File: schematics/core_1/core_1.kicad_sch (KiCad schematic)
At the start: 21 parts, among them U1 74LS00, U2 74LS04, U3 74LS109, U4 74LS02

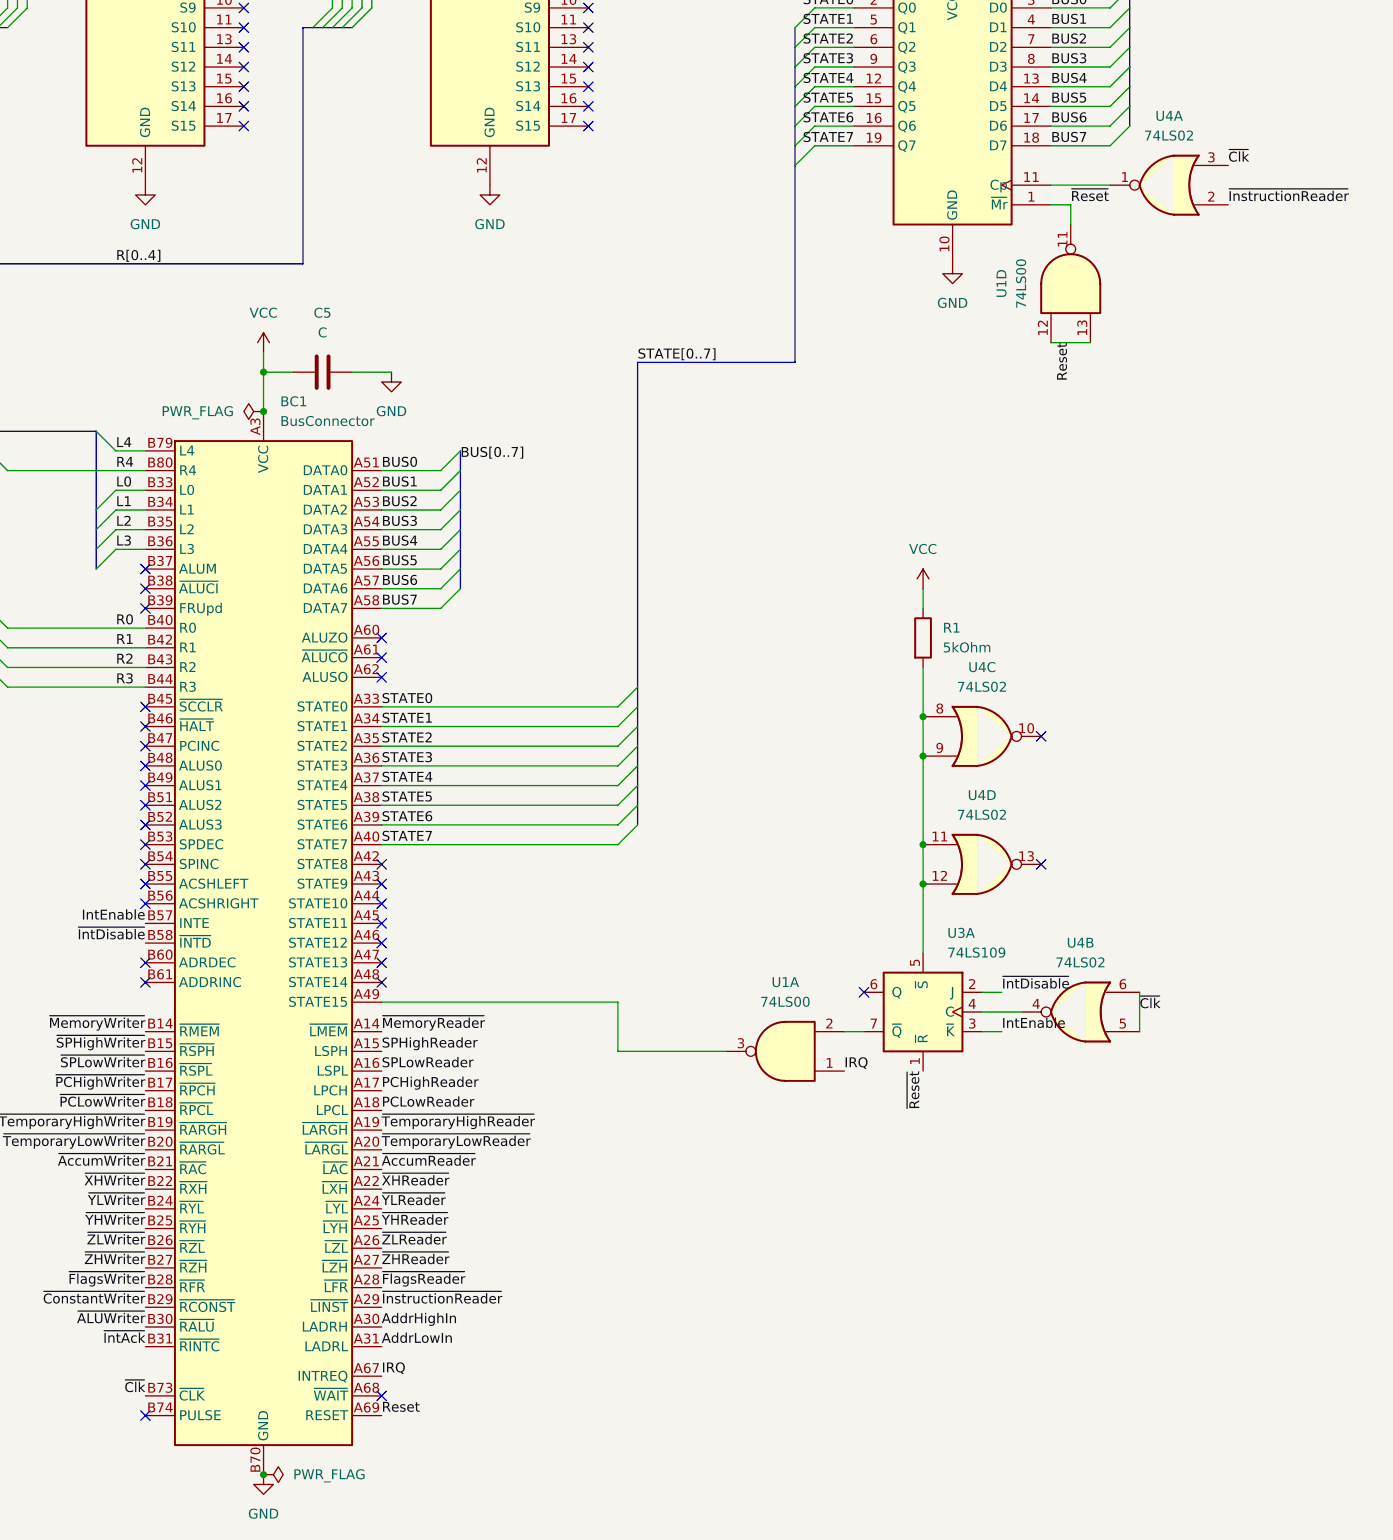
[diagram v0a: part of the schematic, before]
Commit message: Add test points in Core 1
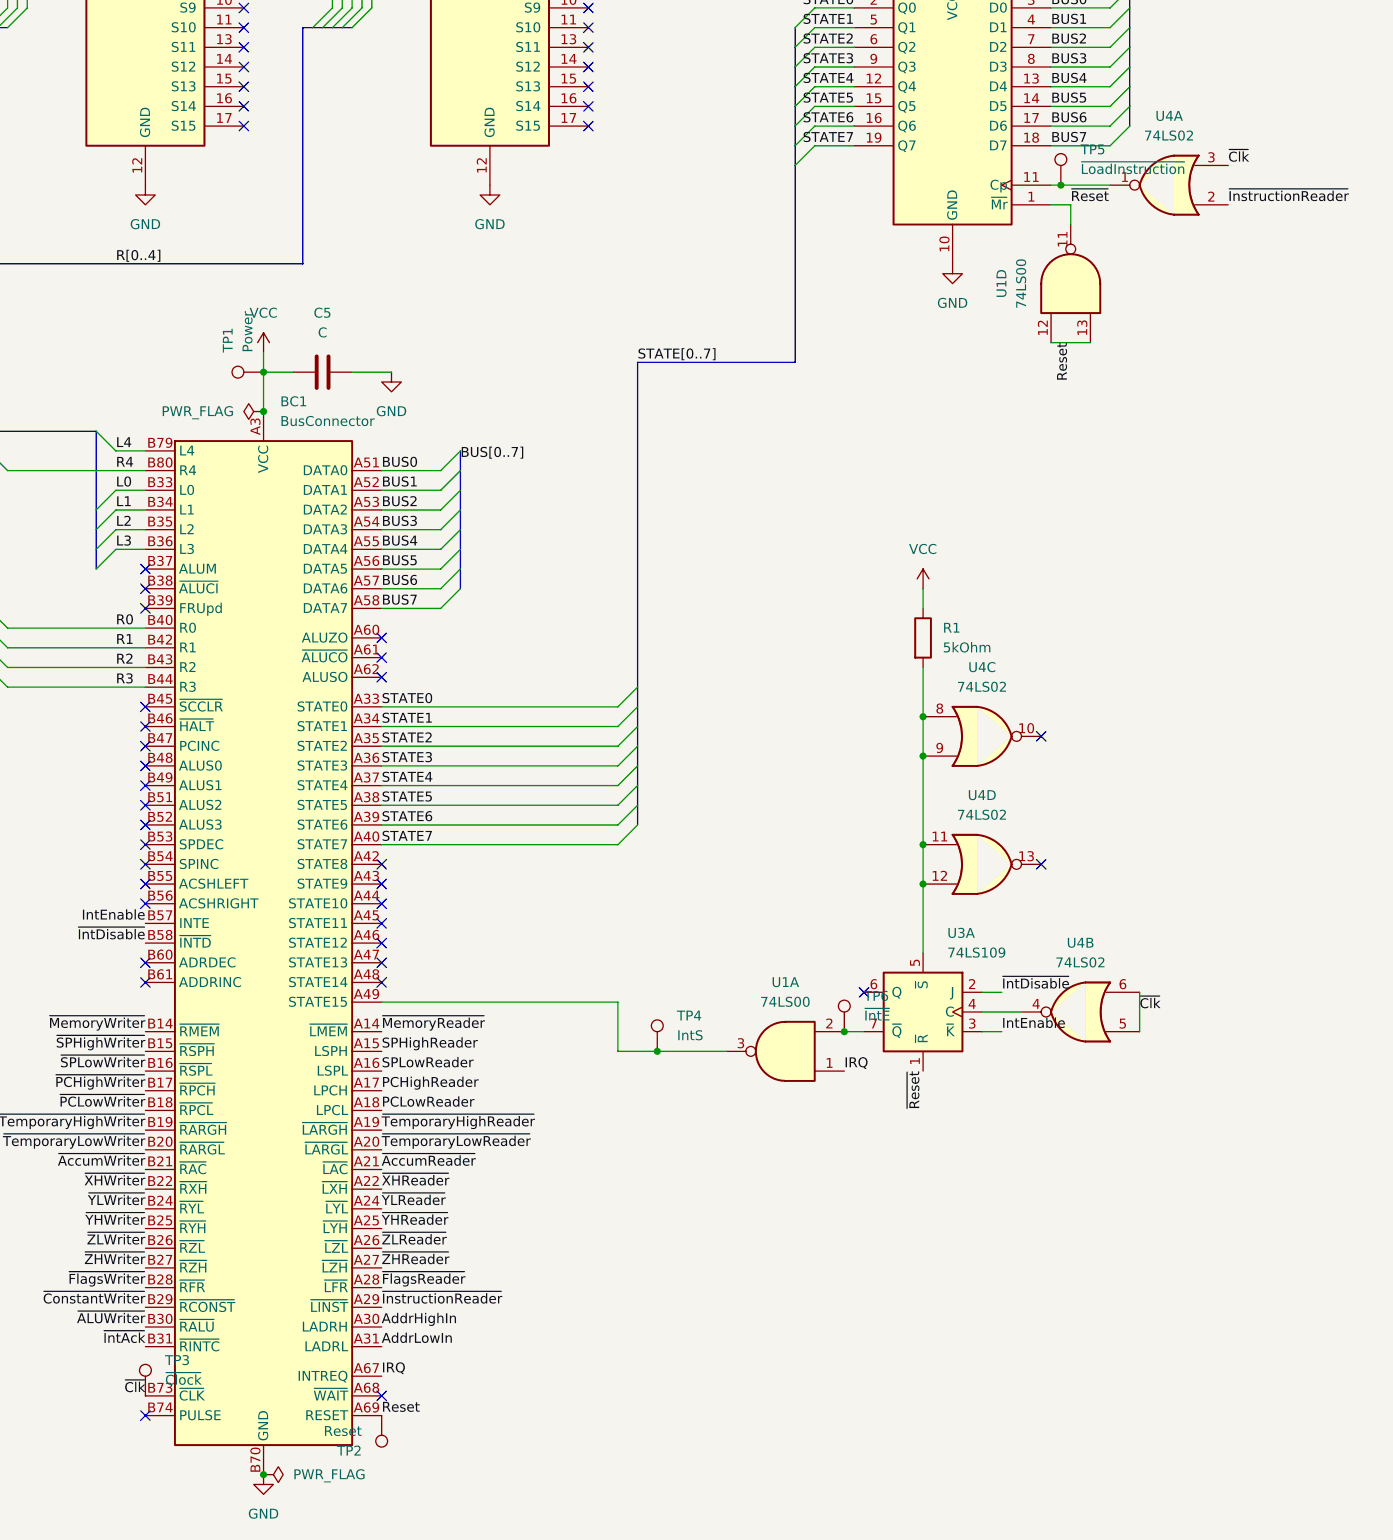
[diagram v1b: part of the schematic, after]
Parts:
- added TP1: Power, Connector_Pin:Pin_D1.0mm_L10.0mm, symbol Connector:TestPoint
- added TP2: Reset, Connector_Pin:Pin_D1.0mm_L10.0mm, symbol Connector:TestPoint
- added TP3: ~{Clock}, Connector_Pin:Pin_D1.0mm_L10.0mm, symbol Connector:TestPoint
- added TP4: IntS, Connector_Pin:Pin_D1.0mm_L10.0mm, symbol Connector:TestPoint
- added TP5: ~{LoadInstruction}, Connector_Pin:Pin_D1.0mm_L10.0mm, symbol Connector:TestPoint
- added TP6: ~{IntE}, Connector_Pin:Pin_D1.0mm_L10.0mm, symbol Connector:TestPoint
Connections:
- net Reset: now also TP2.1
- net VCC: now also TP1.1
- net ~{Clk}: now also TP3.1
- net at INSTRUCTION1.11 (Cp), U4.1: now also TP5.1
- net at BC1.A49 (STATE15), U1.3: now also TP4.1
- net at U1.2, U3.7 (~{Q}): now also TP6.1

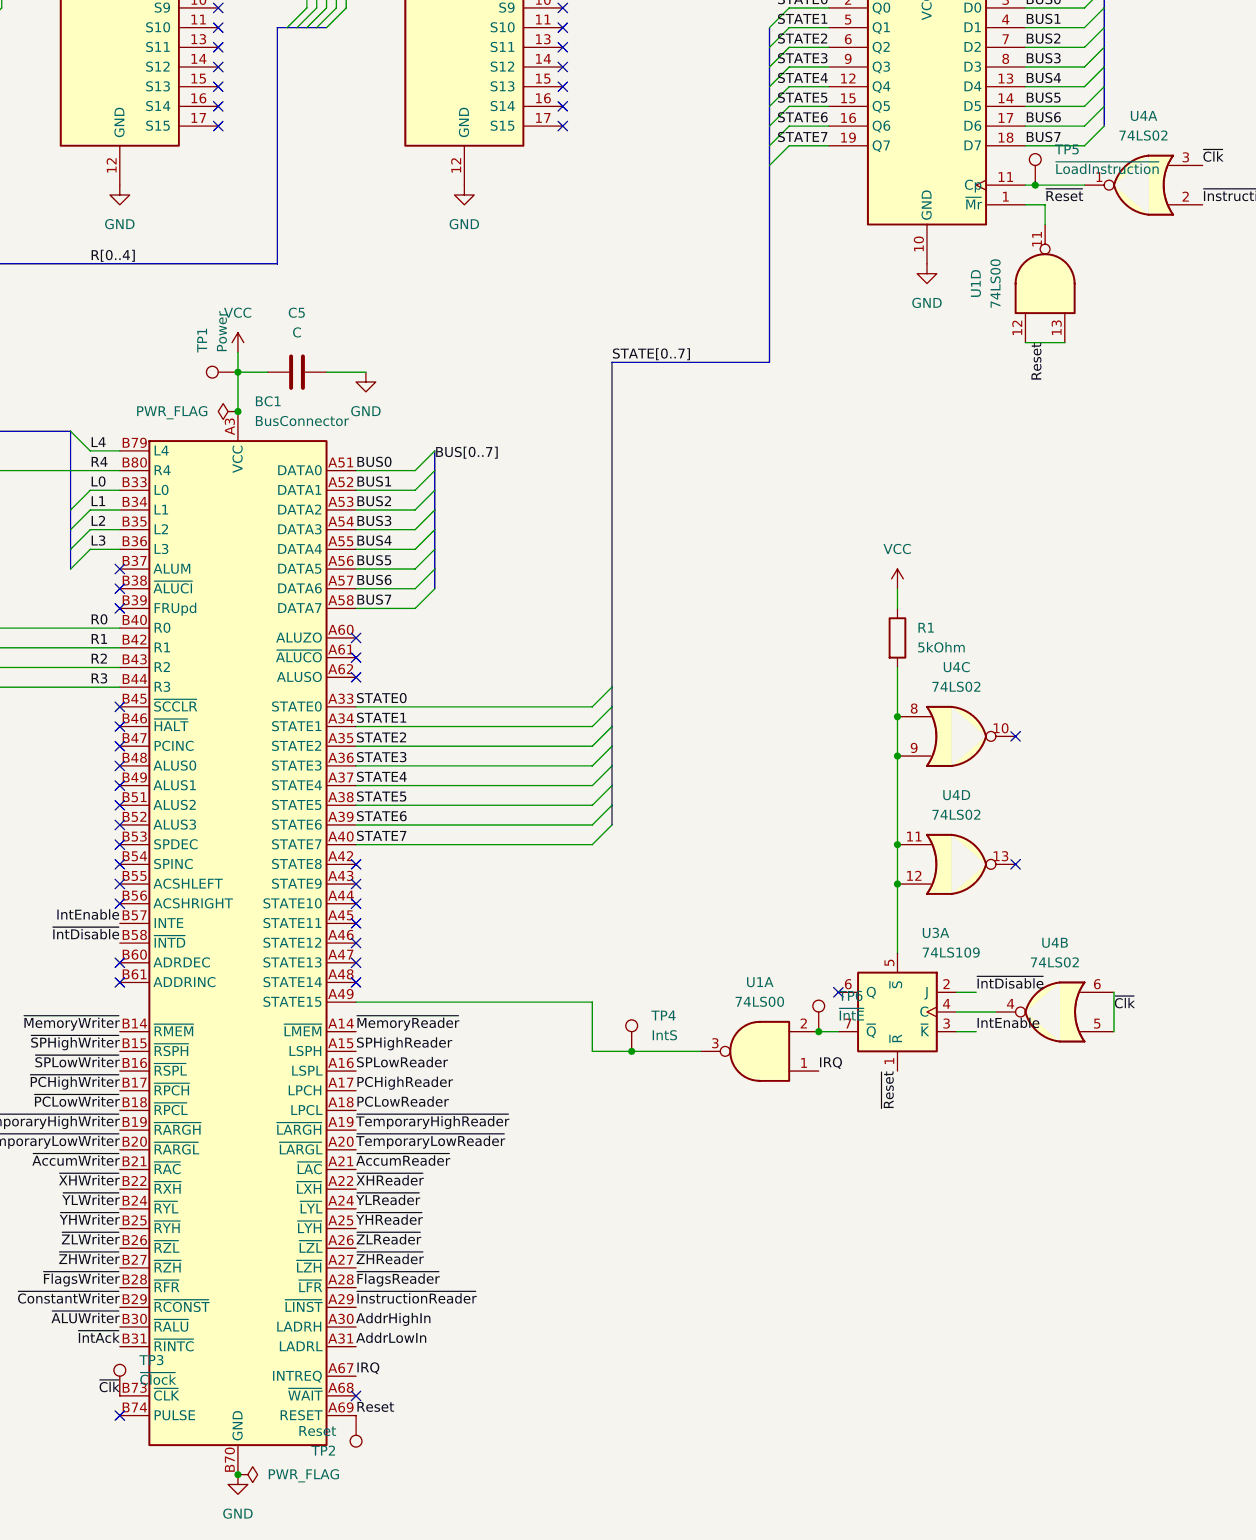
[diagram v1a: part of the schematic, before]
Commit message: Add test points
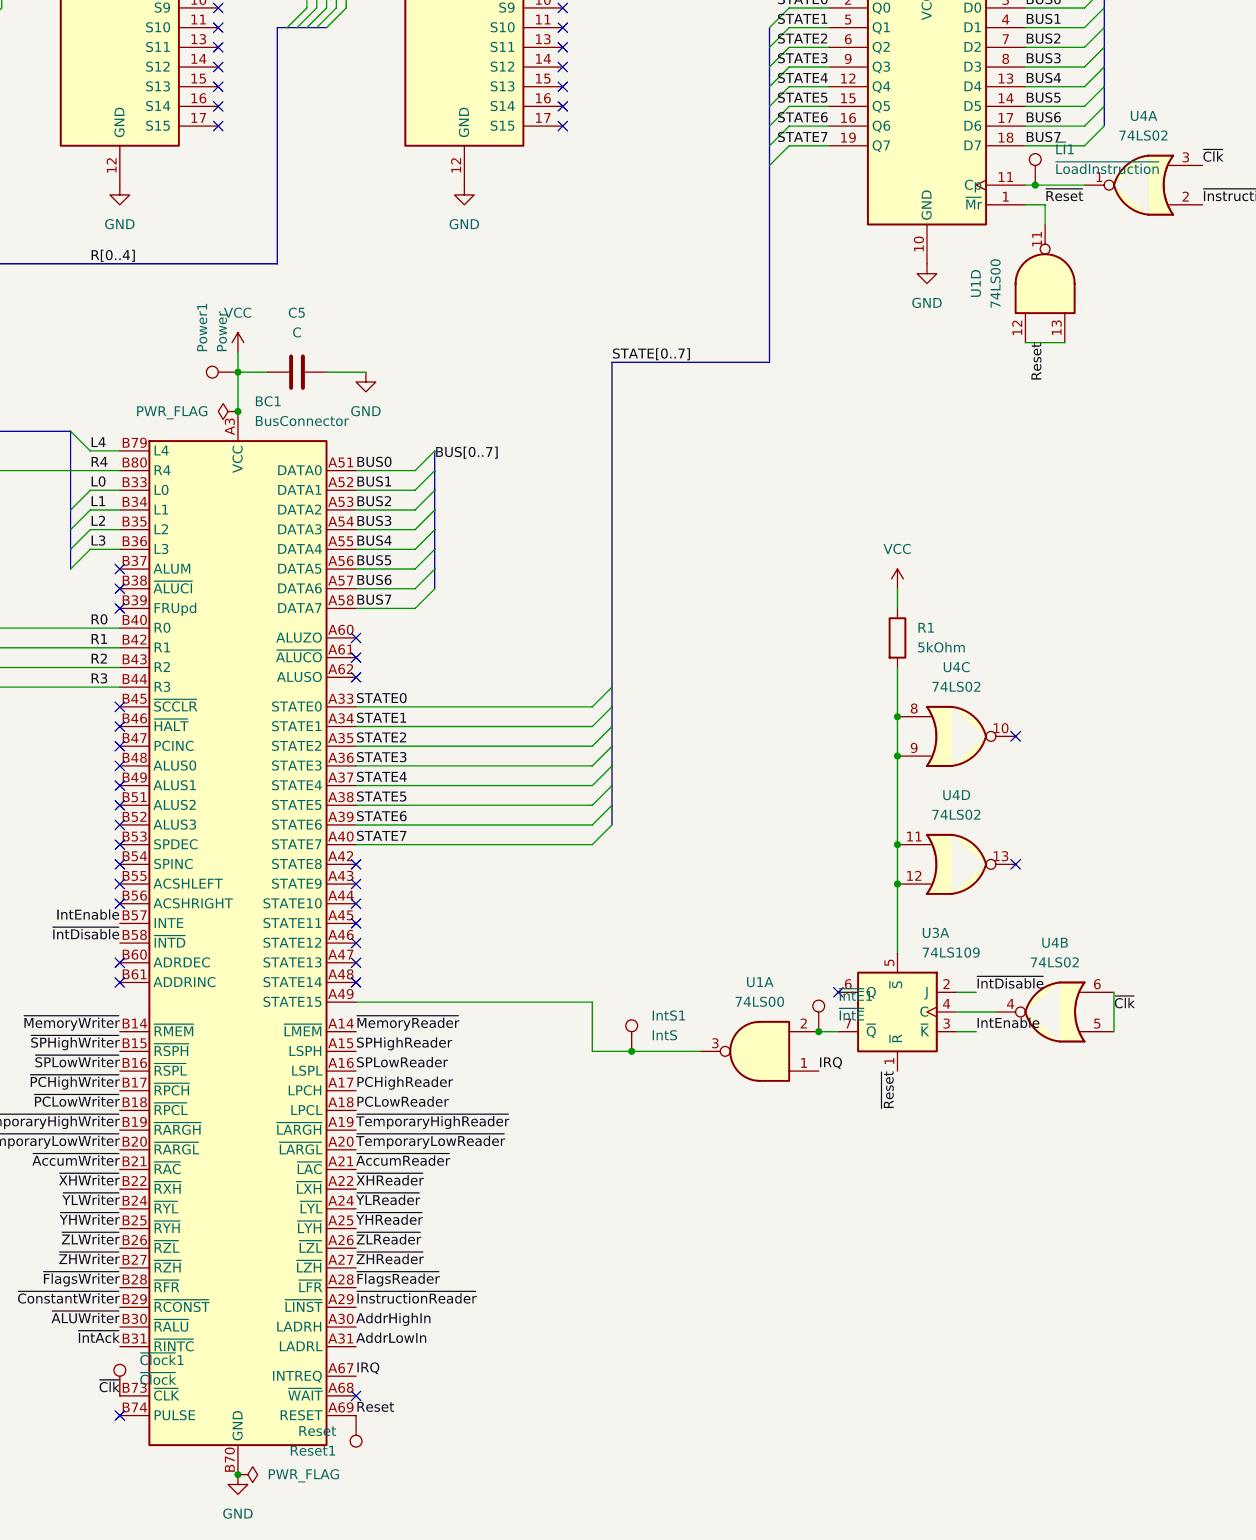
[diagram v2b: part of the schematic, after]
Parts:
- IntS1: renamed from TP4; footprint Connector_Pin:Pin_D1.0mm_L10.0mm -> TestPoint:TestPoint_Pad_D1.0mm
- Power1: renamed from TP1; footprint Connector_Pin:Pin_D1.0mm_L10.0mm -> TestPoint:TestPoint_Pad_D1.0mm
- Reset1: renamed from TP2; footprint Connector_Pin:Pin_D1.0mm_L10.0mm -> TestPoint:TestPoint_Pad_D1.0mm
- ~{Clock}1: renamed from TP3; footprint Connector_Pin:Pin_D1.0mm_L10.0mm -> TestPoint:TestPoint_Pad_D1.0mm
- ~{IntE}1: renamed from TP6; footprint Connector_Pin:Pin_D1.0mm_L10.0mm -> TestPoint:TestPoint_Pad_D1.0mm
- ~{LI}1: renamed from TP5; footprint Connector_Pin:Pin_D1.0mm_L10.0mm -> TestPoint:TestPoint_Pad_D1.0mm
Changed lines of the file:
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@@
 		(on_board yes)
 		(dnp no)
-		(property "Reference" "TP6"
+		(property "Reference" "~{IntE}1"
 			(at 156.21 222.7579 0)
 			(effects
@@
 			)
 		)
-		(property "Footprint" "Connector_Pin:Pin_D1.0mm_L10.0mm"
+		(property "Footprint" "TestPoint:TestPoint_Pad_D1.0mm"
 			(at 158.75 227.33 0)
 			(effects
@@
 			(project "core_1"
 				(path "/17441c17-d186-429b-a2db-836f86810133"
-					(reference "TP6")
+					(reference "~{IntE}1")
 					(unit 1)
 				)
@@
 		(on_board yes)
 		(dnp no)
-		(property "Reference" "TP4"
+		(property "Reference" "IntS1"
 			(at 132.08 225.2979 0)
 			(effects
@@
 			)
 		)
-		(property "Footprint" "Connector_Pin:Pin_D1.0mm_L10.0mm"
+		(property "Footprint" "TestPoint:TestPoint_Pad_D1.0mm"
 			(at 134.62 229.87 0)
 			(effects
@@
 			(project "core_1"
 				(path "/17441c17-d186-429b-a2db-836f86810133"
-					(reference "TP4")
+					(reference "IntS1")
 					(unit 1)
 				)
@@
 		(on_board yes)
 		(dnp no)
-		(property "Reference" "TP1"
+		(property "Reference" "Power1"
 			(at 74.1679 139.7 0)
 			(effects
@@
 			)
 		)
-		(property "Footprint" "Connector_Pin:Pin_D1.0mm_L10.0mm"
+		(property "Footprint" "TestPoint:TestPoint_Pad_D1.0mm"
 			(at 78.74 137.16 0)
 			(effects
@@
 			(project "core_1"
 				(path "/17441c17-d186-429b-a2db-836f86810133"
-					(reference "TP1")
+					(reference "Power1")
 					(unit 1)
 				)
@@
 		(on_board yes)
 		(dnp no)
-		(property "Reference" "TP3"
+		(property "Reference" "~{Clock}1"
 			(at 66.04 269.7479 0)
 			(effects
@@
 			)
 		)
-		(property "Footprint" "Connector_Pin:Pin_D1.0mm_L10.0mm"
+		(property "Footprint" "TestPoint:TestPoint_Pad_D1.0mm"
 			(at 68.58 274.32 0)
 			(effects
@@
 			(project "core_1"
 				(path "/17441c17-d186-429b-a2db-836f86810133"
-					(reference "TP3")
+					(reference "~{Clock}1")
 					(unit 1)
 				)
@@
 		(on_board yes)
 		(dnp no)
-		(property "Reference" "TP5"
+		(property "Reference" "~{LI}1"
 			(at 184.15 113.5379 0)
 			(effects
@@
 			)
 		)
-		(property "Footprint" "Connector_Pin:Pin_D1.0mm_L10.0mm"
+		(property "Footprint" "TestPoint:TestPoint_Pad_D1.0mm"
 			(at 186.69 118.11 0)
 			(effects
@@
 			(project "core_1"
 				(path "/17441c17-d186-429b-a2db-836f86810133"
-					(reference "TP5")
+					(reference "~{LI}1")
 					(unit 1)
 				)
@@
 		(on_board yes)
 		(dnp no)
-		(property "Reference" "TP2"
+		(property "Reference" "Reset1"
 			(at 91.44 281.4321 0)
 			(effects
@@
 			)
 		)
-		(property "Footprint" "Connector_Pin:Pin_D1.0mm_L10.0mm"
+		(property "Footprint" "TestPoint:TestPoint_Pad_D1.0mm"
 			(at 88.9 276.86 0)
 			(effects
@@
 			(project "core_1"
 				(path "/17441c17-d186-429b-a2db-836f86810133"
-					(reference "TP2")
+					(reference "Reset1")
 					(unit 1)
 				)
